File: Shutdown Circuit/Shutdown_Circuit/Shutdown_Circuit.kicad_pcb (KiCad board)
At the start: 2 copper layers, 75 x 80 mm, 23 parts, among them J1 776087-1, K1 V23047A1012A511, K2 V23047A1012A511, K3 V23047A1012A511, Q1 2N2222, Q2 2N2222, Q3 2N2222

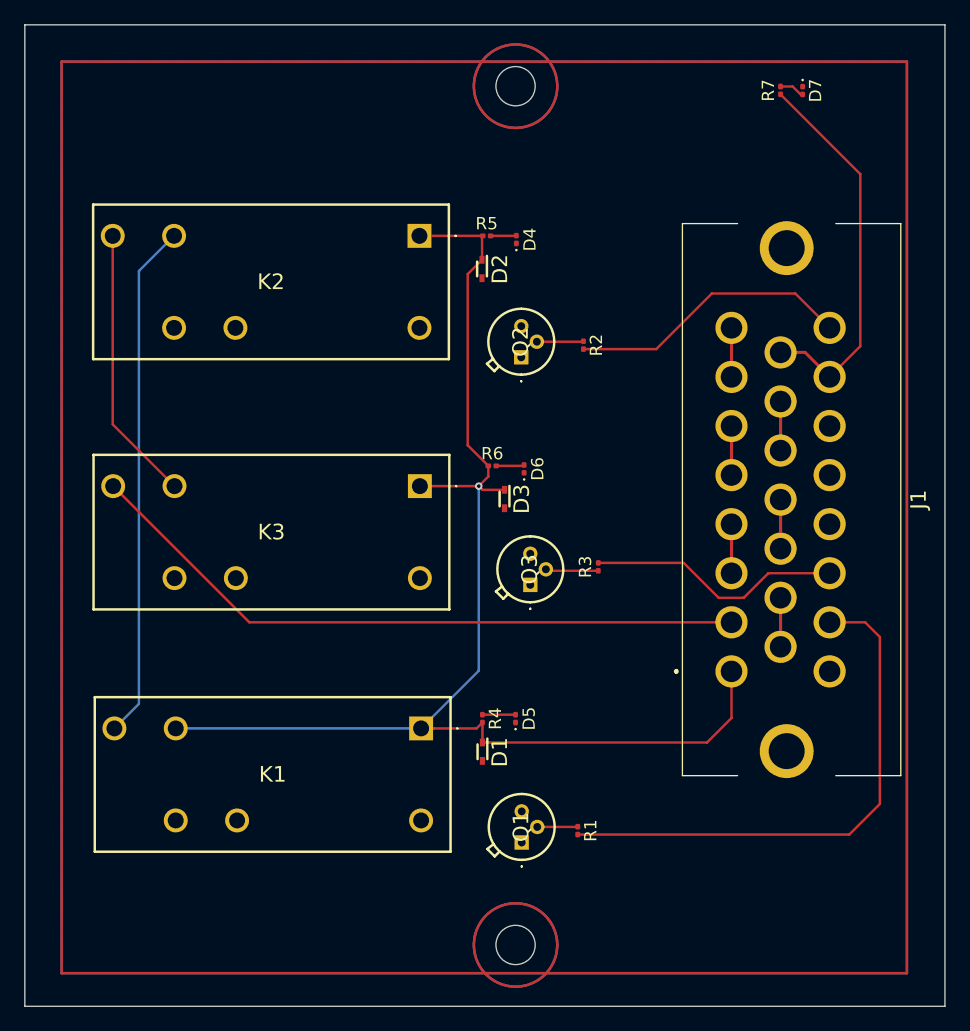
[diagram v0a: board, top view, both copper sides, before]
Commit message: BSPD V1.2, Shutdown Circuit, Charging Shutdown Circuit, Voltage Indicator
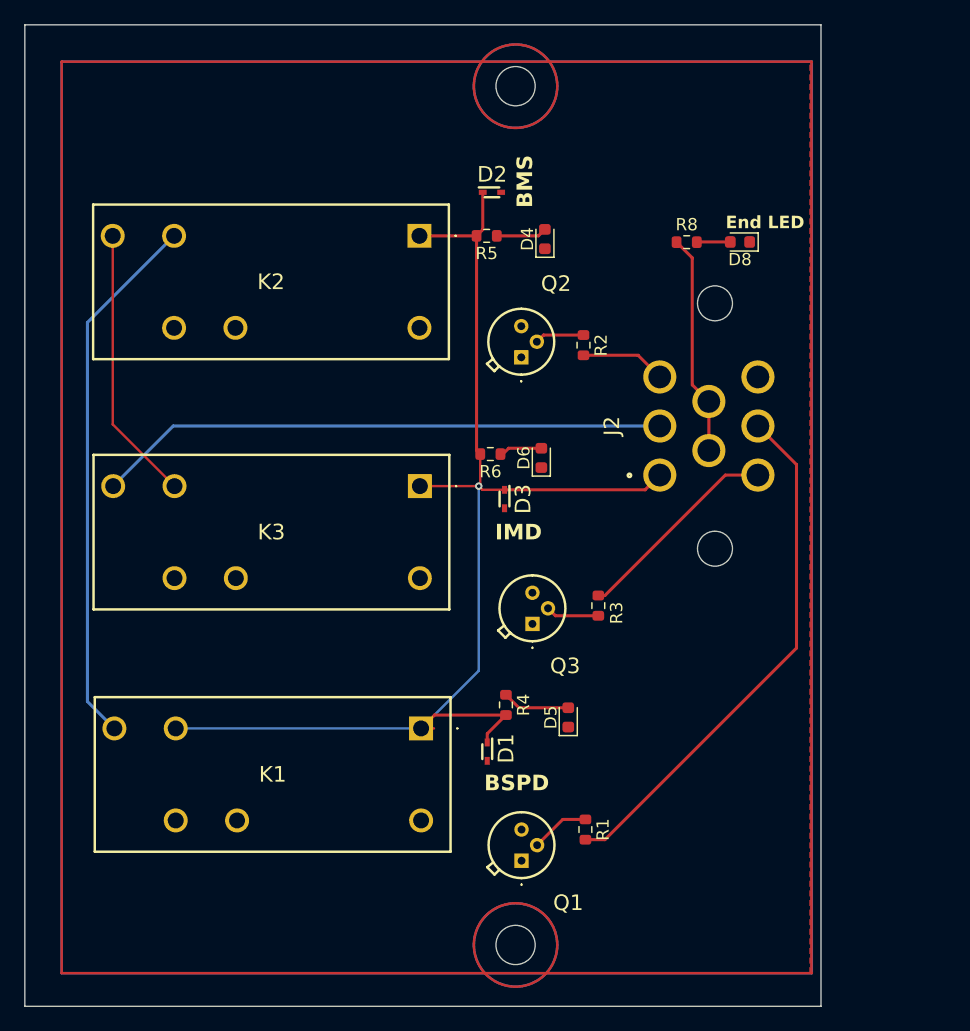
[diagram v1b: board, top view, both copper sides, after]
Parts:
- removed D7: END_CHAIN, LED_SMD:LED_0201_0603Metric
- removed J1: 776087-1, Misc_footprints:7760871
- removed R7: 220, Resistor_SMD:R_0201_0603Metric
- added D8: END_CHAIN, LED_SMD:LED_0603_1608Metric, F.Cu at (134.4, 56.5)
- added J2: 776280-1, SDM_MiscFootprint:776280-1, F.Cu at (143.7, 71.5)
- added R8: 220, Resistor_SMD:R_0603_1608Metric, F.Cu at (130.0, 56.5)
- D4, D5, D6: footprint LED_SMD:LED_0201_0603Metric -> LED_SMD:LED_0603_1608Metric
- R1, R2, R3, R4, R5, R6: footprint Resistor_SMD:R_0201_0603Metric -> Resistor_SMD:R_0603_1608Metric
- moved D2 6.30 mm to (114.2, 52.5), turned to 0 degrees
- moved D5 4.30 mm to (120.4, 95.2)
- moved Q3 3.18 mm to (117.5, 87.6)
- moved R3 3.16 mm to (122.8, 86.1)
- moved D4 2.33 mm to (118.5, 56.3)
- moved R4 2.22 mm to (115.3, 94.2)
- moved D6 1.66 mm to (118.2, 74.1)
- moved Q1 1.48 mm to (116.6, 106.9)
- moved R6 0.98 mm to (114.0, 73.8)
- moved R1 0.63 mm to (121.8, 104.4)
- moved D1 0.39 mm to (113.8, 98.0)
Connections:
- R1 pad 2: BSPD KILL SIGNAL -> /BSPD KILL SIGNAL
- R2 pad 2: BMS KILL SIGNAL -> /BMS KILL SIGNAL
- R3 pad 2: IMD KILL SIGNAL -> /IMD KILL SIGNAL
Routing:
- net BSPD KILL SIGNAL: track 43.9 -> 0.00 mm
- net /BSPD KILL SIGNAL: track 0.00 -> 43.1 mm
- net SHUTDOWN_OUT: track 31.6 -> 0.00 mm
- net BMS KILL SIGNAL: track 23.1 -> 0.00 mm
- net IMD KILL SIGNAL: track 20.9 -> 0.00 mm
- net AIR SIGNAL: track 0.00 -> 18.1 mm
- net /IMD KILL SIGNAL: track 0.00 -> 17.1 mm
- net /RELAYS_OUT: track 55.0 -> 46.6 mm
- net /BMS KILL SIGNAL: track 0.00 -> 6.95 mm
- net +12V: track 107.6 -> 102.1 mm
- net Net-(J1-Pad7): track 4.00 -> 0.00 mm
- net Net-(J1-Pad5): track 4.00 -> 0.00 mm
- net Net-(J1-Pad3): track 4.00 -> 0.00 mm
- net Net-(J1-Pad13): track 4.00 -> 0.00 mm
- net Net-(J1-Pad11): track 4.00 -> 0.00 mm
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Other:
- board size 75 x 80 mm -> 64.9 x 80 mm
- board text added: "BMS"
- board text added: "BSPD"
- board text added: "End LED"
- board text added: "IMD"

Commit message: BSPD, Shutdown/Charging Shutdown, & Voltage Indicator final changes
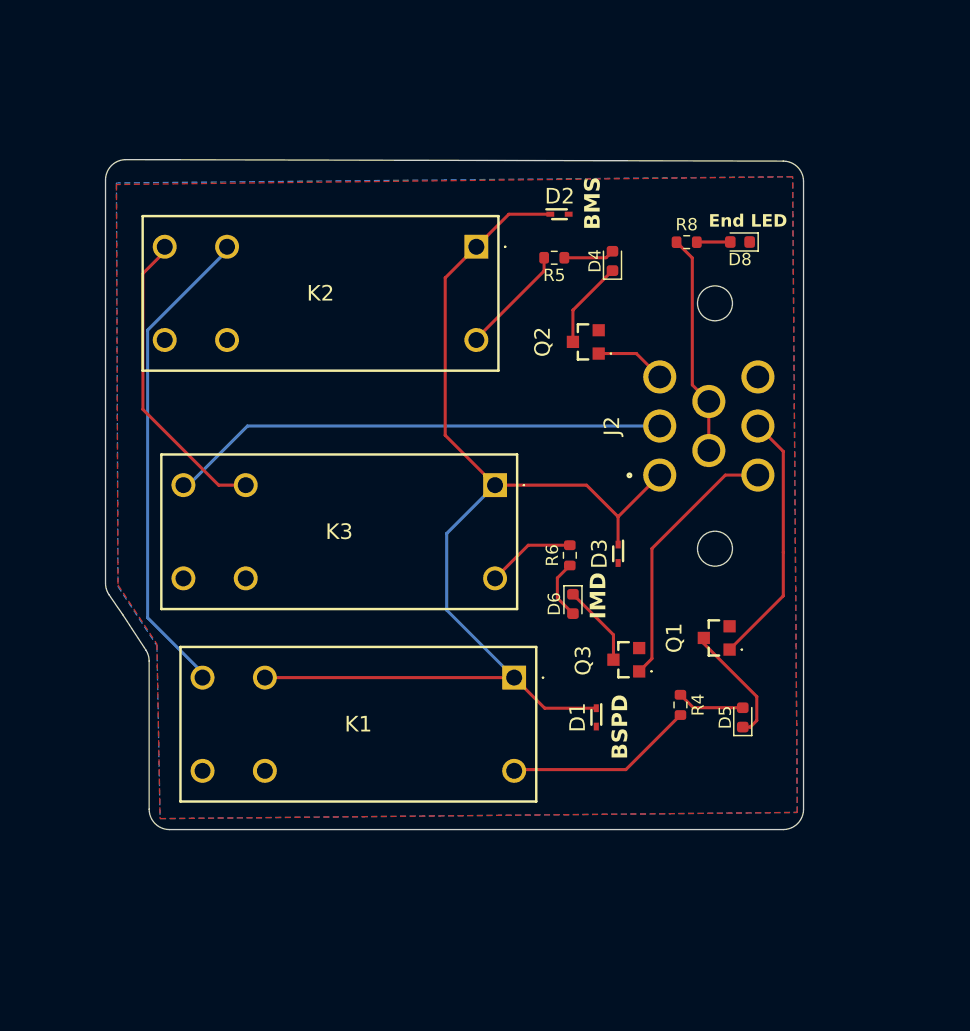
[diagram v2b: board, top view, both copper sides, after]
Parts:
- removed R1, R2, R3: 680, Resistor_SMD:R_0603_1608Metric
- removed REF** (x2): MountingHole_3.2mm_M3, MountingHole:MountingHole_3.2mm_M3
- K1, K2, K3: value V23047A1012A511 -> PR22-12V-400-1A; footprint Misc_footprints:V23047A1012A511 -> Misc_footprints:PR2212V4001A
- Q1, Q2, Q3: value 2N2222 -> ZXM61N02FTC; footprint Package_TO_SOT_THT:2N2222 -> Misc_footprints:ZXM61N02FTC
- R4, R5, R6: value 220 -> 680
- moved Q1 24.1 mm to (132.5, 88.8)
- moved D5 14.2 mm to (134.6, 95.2)
- moved R4 14.2 mm to (129.5, 94.2)
- moved D6 12.2 mm to (120.8, 86.0), turned to -90 degrees
- moved R6 10.5 mm to (120.5, 82.0), turned to 90 degrees
- moved D3 10.3 mm to (124.5, 81.9)
- moved D1 9.32 mm to (122.7, 95.2)
- moved K1 8.64 mm to (116.0, 92.0)
- moved Q3 8.19 mm to (125.1, 90.6)
- moved K3 6.13 mm to (114.4, 76.3)
- moved D2 5.79 mm to (119.7, 54.2)
- moved D4 5.79 mm to (124.0, 58.0)
- moved R5 5.79 mm to (119.3, 57.8)
- moved Q2 5.41 mm to (121.8, 64.6)
- moved K2 4.72 mm to (112.9, 56.9)
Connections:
- D4 pad 1: GND -> Net-(D4-K)
- D5 pad 1: GND -> Net-(D5-K)
- D6 pad 1: GND -> Net-(D6-K)
- K1 pad 2: GND -> +12V
- K2 pad 2: GND -> Net-(K1-NO_1)
- K3 pad 2: GND -> Net-(K2-NO_1)
- Q1 pad 1: GND -> /BSPD KILL SIGNAL
- Q1 pad 2: Net-(Q1-B) -> Net-(D5-K)
- Q2 pad 1: GND -> /BMS KILL SIGNAL
- Q2 pad 2: Net-(Q2-B) -> Net-(D4-K)
- Q3 pad 1: GND -> /IMD KILL SIGNAL
- Q3 pad 2: Net-(Q3-B) -> Net-(D6-K)
- R4 pad 2: +12V -> Net-(K1-COIL_2)
- R5 pad 2: +12V -> Net-(K2-COIL_2)
- R6 pad 2: +12V -> Net-(K3-COIL_2)
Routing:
- net /BSPD KILL SIGNAL: track 43.1 -> 20.9 mm
- net Net-(K1-COIL_2): track 0.00 -> 15.4 mm
- net Net-(D5-K): track 0.00 -> 9.88 mm
- net Net-(K2-COIL_2): track 0.00 -> 8.89 mm
- net +12V: track 102.1 -> 94.8 mm, vias 1 -> 0
- net Net-(K3-COIL_2): track 0.00 -> 7.22 mm
- net Net-(D4-K): track 0.00 -> 7.14 mm
- net Net-(D6-K): track 0.00 -> 6.70 mm
- net /RELAYS_OUT: track 46.6 -> 40.4 mm
- net Net-(Q1-B): track 4.80 -> 0.00 mm
- net /IMD KILL SIGNAL: track 17.1 -> 21.6 mm
- net Net-(Q3-B): track 4.35 -> 0.00 mm
- net Net-(K1-NO_1): track 44.0 -> 40.0 mm
- net Net-(Q2-B): track 4.03 -> 0.00 mm
- net Net-(K2-NO_1): track 22.5 -> 25.4 mm
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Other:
- board size 64.9 x 80 mm -> 56.9 x 54.6 mm
